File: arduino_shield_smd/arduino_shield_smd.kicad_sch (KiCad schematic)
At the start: 35 parts, among them J1 Power, J2 Digital/PWM, J3 Analog, J4 Digital/PWM, U1 ULN2803A, U2 ULN2803A, U3 PCF8574T, U4 PCF8574T

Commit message: second commit
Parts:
- added C4, C5, C6: 1uF, symbol Device:C_Small
- added D4: 2A, symbol Device:D
- added RN1, RN2, RN3, RN4: 1K, symbol Device:R_Pack04
- C2: renamed from C?; value 1uF -> 100nF
- C3: renamed from C?; value 10uF -> 22uF
- JA5: renamed from JP5; value 1X10 2.5mm -> HNC2-2.5P-10DS(55); footprint ayab-library:SHDR10W70P0X250_1X10_2740X490X590P -> ayab-library:Molex_0022035105 or Hirose_HNC2-2.5P-10DS
- R1: renamed from R3; value 100 -> 150
- R4: renamed from R1; value 5K -> 4.7K
- R5: renamed from R2; value 5K -> 4.7K
- gave numbers to parts that had none: 1
- renumbered JP2 to JA2, JP3 to JA3, JP4 to JA4, JP7 to JA7, JP8 to JA8, JP2A0 to JB2, JP3A0 to JB3, JP4A0 to JB4, JP7A0 to JB7, JP8A0 to JB8, R5 to R2, R4 to R3, U4 to U1, U1 to U4
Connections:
- net +5V: now also C5.1, C6.1, RN1.5 (R4.2), RN1.6 (R3.2), RN1.7 (R2.2), RN1.8 (R1.2), RN2.5 (R4.2), RN2.6 (R3.2), RN2.7 (R2.2), RN2.8 (R1.2), RN3.5 (R4.2), RN3.6 (R3.2), RN3.7 (R2.2), RN3.8 (R1.2), RN4.5 (R4.2), RN4.6 (R3.2), RN4.7 (R2.2), RN4.8 (R1.2)
- net GND: now also C4.2, C5.2, C6.2, D4.2 (A)
- net VIN: now also C4.1, D4.1 (K)
- net at U1.10 (P5), U2.6 (I6): now also RN2.2 (R2.1)
- net at U1.11 (P6), U2.7 (I7): now also RN2.3 (R3.1)
- net at U1.12 (P7), U2.8 (I8): now also RN2.4 (R4.1)
- net at U1.4 (P0), U2.1 (I1): now also RN1.1 (R1.1)
- net at U1.5 (P1), U2.2 (I2): now also RN1.2 (R2.1)
- net at U1.6 (P2), U2.3 (I3): now also RN1.3 (R3.1)
- net at U1.7 (P3), U2.4 (I4): now also RN1.4 (R4.1)
- net at U1.9 (P4), U2.5 (I5): now also RN2.1 (R1.1)
- net at U3.4 (P0), U4.1 (I1): now also RN3.1 (R1.1)
- net at U3.5 (P1), U4.2 (I2): now also RN3.2 (R2.1)
- net at U3.6 (P2), U4.3 (I3): now also RN3.3 (R3.1)
- net at U3.7 (P3), U4.4 (I4): now also RN3.4 (R4.1)
- net at U3.9 (P4), U4.5 (I5): now also RN4.1 (R1.1)
- net at U3.10 (P5), U4.6 (I6): now also RN4.2 (R2.1)
- net at U3.11 (P6), U4.7 (I7): now also RN4.3 (R3.1)
- net at U3.12 (P7), U4.8 (I8): now also RN4.4 (R4.1)
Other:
- note added: "JB2"
- note added: "JB3"
- note added: "JB4"
- note added: "JB7"
- note added: "JB8"
- note removed: "JP2A"
- note removed: "JP3A"
- note removed: "JP4A"
- note removed: "JP7A"
- note removed: "JP8A"
- moved on the sheet: C1, C2, C3, JA3, JA4, JA5, JA7, JA8, TP1, TP2, TP3, U1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

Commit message: OSHpark prototype
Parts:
- removed D4: 2A, symbol Device:D
- renumbered JP9 to J5, JP6 to J6
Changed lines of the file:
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@@
 	(wire
 		(pts
-			(xy 41.91 139.7) (xy 50.8 139.7)
-		)
-		(stroke
-			(width 0)
-			(type default)
-		)
-	)
-	(wire
-		(pts
 			(xy 182.88 146.05) (xy 182.88 143.51)
 		)
@@
 	(wire
 		(pts
-			(xy 41.91 132.08) (xy 50.8 132.08)
-		)
-		(stroke
-			(width 0)
-			(type default)
-		)
-	)
-	(wire
-		(pts
 			(xy 83.82 166.37) (xy 99.06 166.37)
 		)
@@
 	)
 	(symbol
-		(lib_id "Device:D")
-		(at 41.91 135.89 270)
-		(unit 1)
-		(exclude_from_sim no)
-		(in_bom yes)
-		(on_board yes)
-		(dnp no)
-		(fields_autoplaced yes)
-		(property "Reference" "D4"
-			(at 44.45 134.6199 90)
-			(effects
-				(font
-					(size 1.27 1.27)
-				)
-				(justify left)
-			)
-		)
-		(property "Value" "2A"
-			(at 44.45 137.1599 90)
-			(effects
-				(font
-					(size 1.27 1.27)
-				)
-				(justify left)
-			)
-		)
-		(property "Footprint" ""
-			(at 41.91 135.89 0)
-			(effects
-				(font
-					(size 1.27 1.27)
-				)
-				(hide yes)
-			)
-		)
-		(property "Datasheet" "~"
-			(at 41.91 135.89 0)
-			(effects
-				(font
-					(size 1.27 1.27)
-				)
-				(hide yes)
-			)
-		)
-		(property "Description" "Diode"
-			(at 41.91 135.89 0)
-			(effects
-				(font
-					(size 1.27 1.27)
-				)
-				(hide yes)
-			)
-		)
-		(property "Sim.Device" "D"
-			(at 41.91 135.89 0)
-			(effects
-				(font
-					(size 1.27 1.27)
-				)
-				(hide yes)
-			)
-		)
-		(property "Sim.Pins" "1=K 2=A"
-			(at 41.91 135.89 0)
-			(effects
-				(font
-					(size 1.27 1.27)
-				)
-				(hide yes)
-			)
-		)
-		(pin "1"
-		)
-		(pin "2"
-		)
-		(instances
-			(project ""
-				(path "/dc4e9b16-0d76-4cba-8254-625ae2e12c75"
-					(reference "D4")
-					(unit 1)
-				)
-			)
-		)
-	)
-	(symbol
 		(lib_id "ayab-lib:Conn_01x08")
 		(at 256.54 97.79 0)
@@
 		(on_board yes)
 		(dnp no)
-		(property "Reference" "JP6"
+		(property "Reference" "J6"
 			(at 107.95 63.5 90)
 			(effects
@@
 			(project ""
 				(path "/dc4e9b16-0d76-4cba-8254-625ae2e12c75"
-					(reference "JP6")
+					(reference "J6")
 					(unit 1)
 				)
@@
 		(on_board yes)
 		(dnp no)
-		(property "Reference" "JP9"
+		(property "Reference" "J5"
 			(at 237.49 135.89 0)
 			(effects
@@
 			(project ""
 				(path "/dc4e9b16-0d76-4cba-8254-625ae2e12c75"
-					(reference "JP9")
+					(reference "J5")
 					(unit 1)
 				)

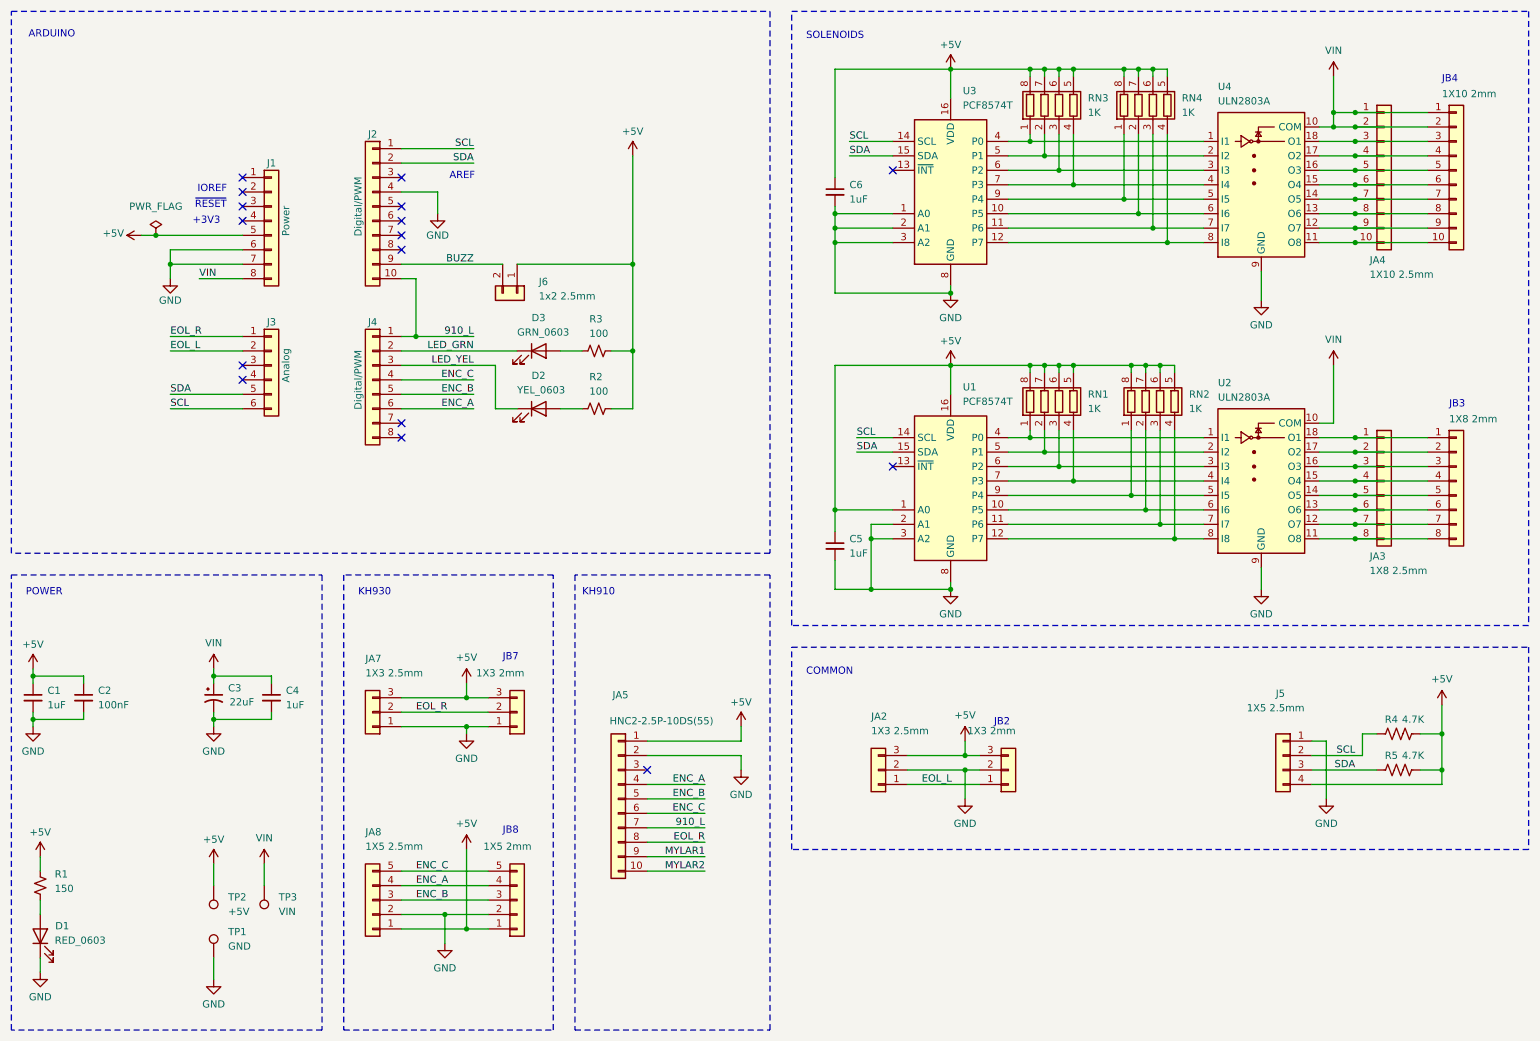
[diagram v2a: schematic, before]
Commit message: Add change LED footprints and add blue LED
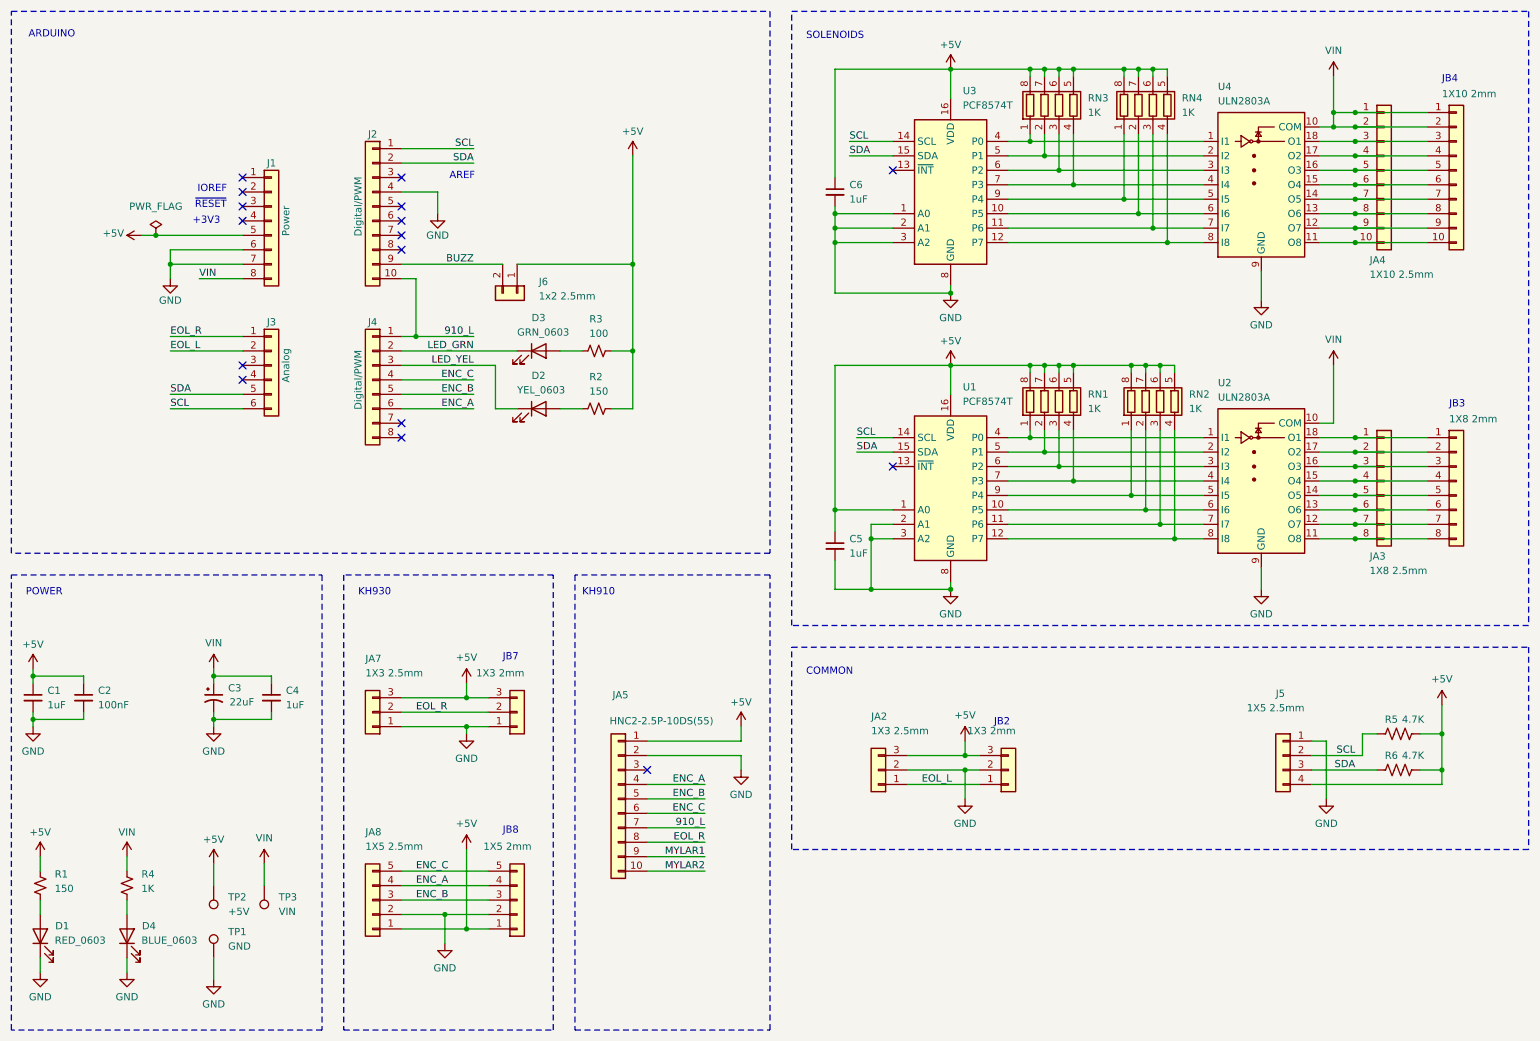
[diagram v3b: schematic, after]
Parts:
- added D4: BLUE_0603, LED_SMD:LED_0805_2012Metric, symbol ayab-lib:LED
- added R4: 1K, Resistor_SMD:R_0805_2012Metric, symbol ayab-lib:R_Small_US
- C1, C4, C5, C6: footprint (none) -> Capacitor_SMD:C_1206_3216Metric
- C2: footprint (none) -> Capacitor_SMD:C_0603_1608Metric
- C3: footprint (none) -> Capacitor_Tantalum_SMD:CP_EIA-3528-15_AVX-H
- D1: footprint LED_THT:LED_D3.0mm -> LED_SMD:LED_0805_2012Metric; Mfg Broadcom -> (none); Mfg P/N HLMP-NG07 -> (none)
- D2: footprint LED_THT:LED_D3.0mm -> LED_SMD:LED_0805_2012Metric; Mfg Broadcom -> (none); Mfg P/N HLMP-NL06 -> (none)
- D3: footprint LED_THT:LED_D3.0mm -> LED_SMD:LED_0805_2012Metric; Mfg Broadcom -> (none); Mfg P/N HLMP-1640-B00A1 -> (none)
- J1, J4: footprint Connector_PinSocket_2.54mm:PinSocket_1x08_P2.54mm_Vertical -> Connector_PinHeader_2.54mm:PinHeader_1x08_P2.54mm_Vertical
- J2: footprint Connector_PinSocket_2.54mm:PinSocket_1x10_P2.54mm_Vertical -> Connector_PinHeader_2.54mm:PinHeader_1x10_P2.54mm_Vertical
- J3: footprint Connector_PinSocket_2.54mm:PinSocket_1x06_P2.54mm_Vertical -> Connector_PinHeader_2.54mm:PinHeader_1x06_P2.54mm_Vertical
- J5: footprint Connector_PinHeader_2.54mm:PinHeader_1x04_P2.54mm_Vertical -> ayab-library:PinHeader_1x04_P2.54mm_Vertical
- J6: footprint Connector_PinHeader_2.54mm:PinHeader_1x02_P2.54mm_Vertical -> ayab-library:PinHeader_1x02_P2.54mm_Vertical
- JA2: footprint ayab-library:SHDR3W70P0X250_1X3_990X490X590P -> ayab-library:Molex_0022035035 or Hirose_HNC2-2.5P-3DS
- JA3: footprint ayab-library:SHDR8W65P0X250_1X8_2240X490X610P -> ayab-library:Molex_0022035085 or Hirose_HNC2_2.5P_8DS
- JA4: footprint ayab-library:SHDR10W70P0X250_1X10_2740X490X590P -> ayab-library:Molex_0022035105 or Hirose_HNC2-2.5P-10DS
- JA5: footprint ayab-library:Molex_0022035105 or Hirose_HNC2-2.5P-10DS -> ayab-library:HNC2-2.5P-10DS
- JA7: footprint ayab-library:SHDR3W70P0X250_1X3_990X490X590P -> ayab-library:Molex_SPOX_5267-03A_1x03_P2.50mm_Vertical
- JA8: footprint ayab-library:99990989 -> ayab-library:Molex_SPOX_5267-05A_1x05_P2.50mm_Vertical
- JB2, JB7: LCSC ID (none) -> C225241; OEM (none) -> CJT(Changjiang Connectors); OEM PN (none) -> A2004WV-3P
- JB3: LCSC ID (none) -> C225246; OEM (none) -> CJT(Changjiang Connectors); OEM PN (none) -> A2004WV-8P
- JB8: LCSC ID (none) -> C225243; OEM (none) -> CJT(Changjiang Connectors); OEM PN (none) -> A2004WV-5P
- R1, R3: footprint Resistor_THT:R_Axial_DIN0204_L3.6mm_D1.6mm_P2.54mm_Vertical -> Resistor_SMD:R_0805_2012Metric
- R2: value 100 -> 150; footprint Resistor_THT:R_Axial_DIN0204_L3.6mm_D1.6mm_P2.54mm_Vertical -> Resistor_SMD:R_0805_2012Metric
- R5: renamed from R4; footprint (none) -> Resistor_SMD:R_0805_2012Metric
- R6: renamed from R5; footprint (none) -> Resistor_SMD:R_0805_2012Metric
- RN1, RN2, RN3, RN4: footprint (none) -> Resistor_SMD:R_Array_Convex_4x0603
- TP1, TP2, TP3: footprint (none) -> TestPoint:TestPoint_THTPad_3.0x3.0mm_Drill1.5mm
- U2, U4: footprint Package_DIP:DIP-18_W7.62mm_LongPads -> Package_SO:SOIC-18W_7.5x11.6mm_P1.27mm
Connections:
- net GND: now also D4.1 (K)
- net VIN: now also R4.1
- new net: D4.2 (A), R4.2

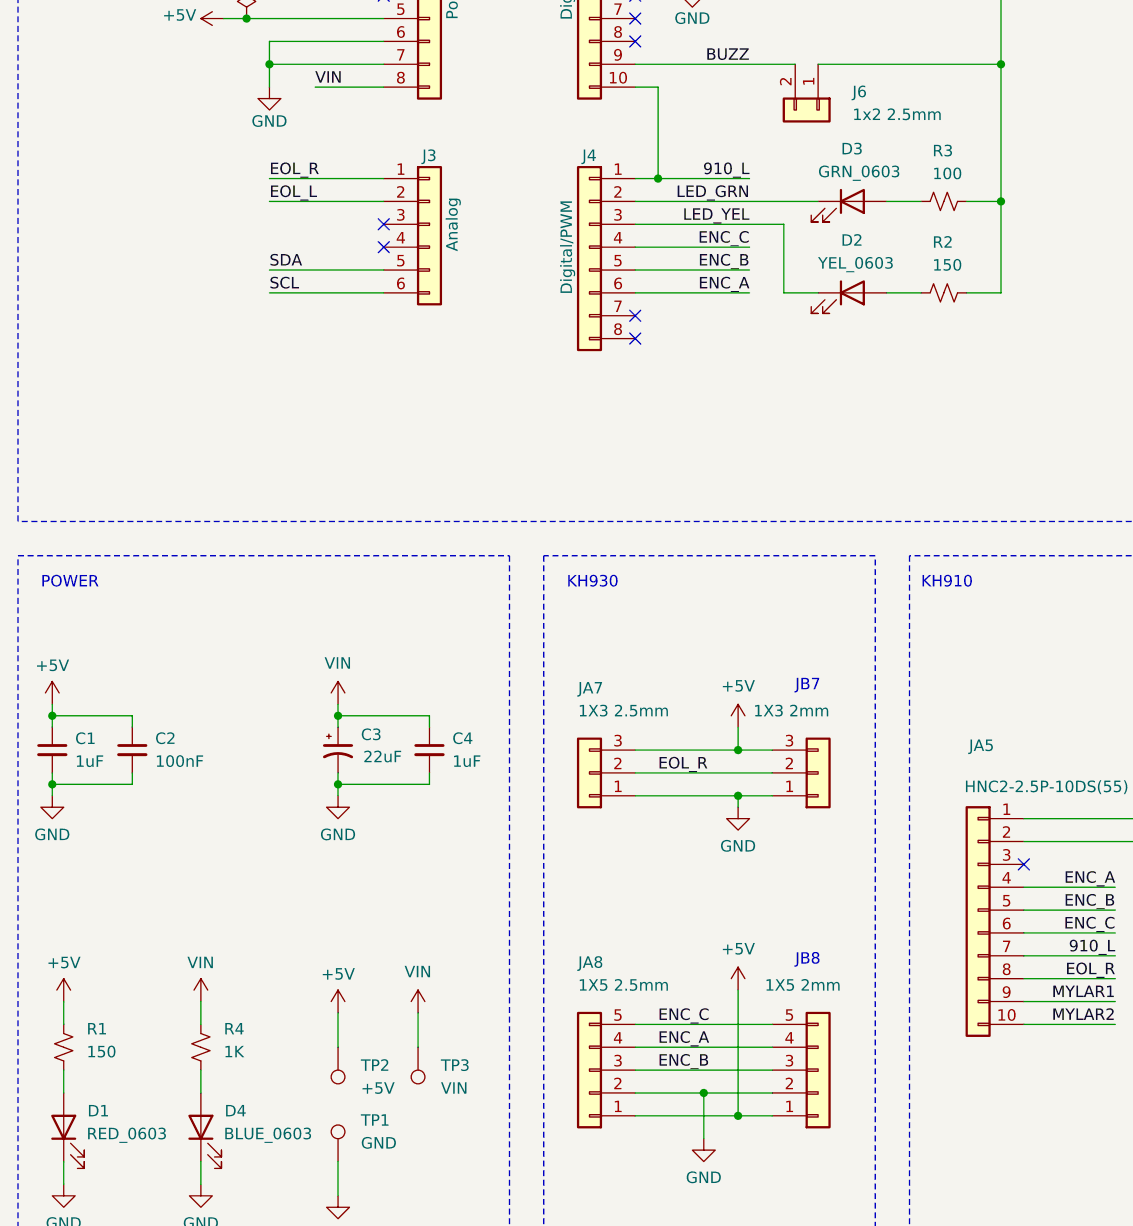
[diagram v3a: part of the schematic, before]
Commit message: Increase LED series resistor values to support Arduino Uno R4
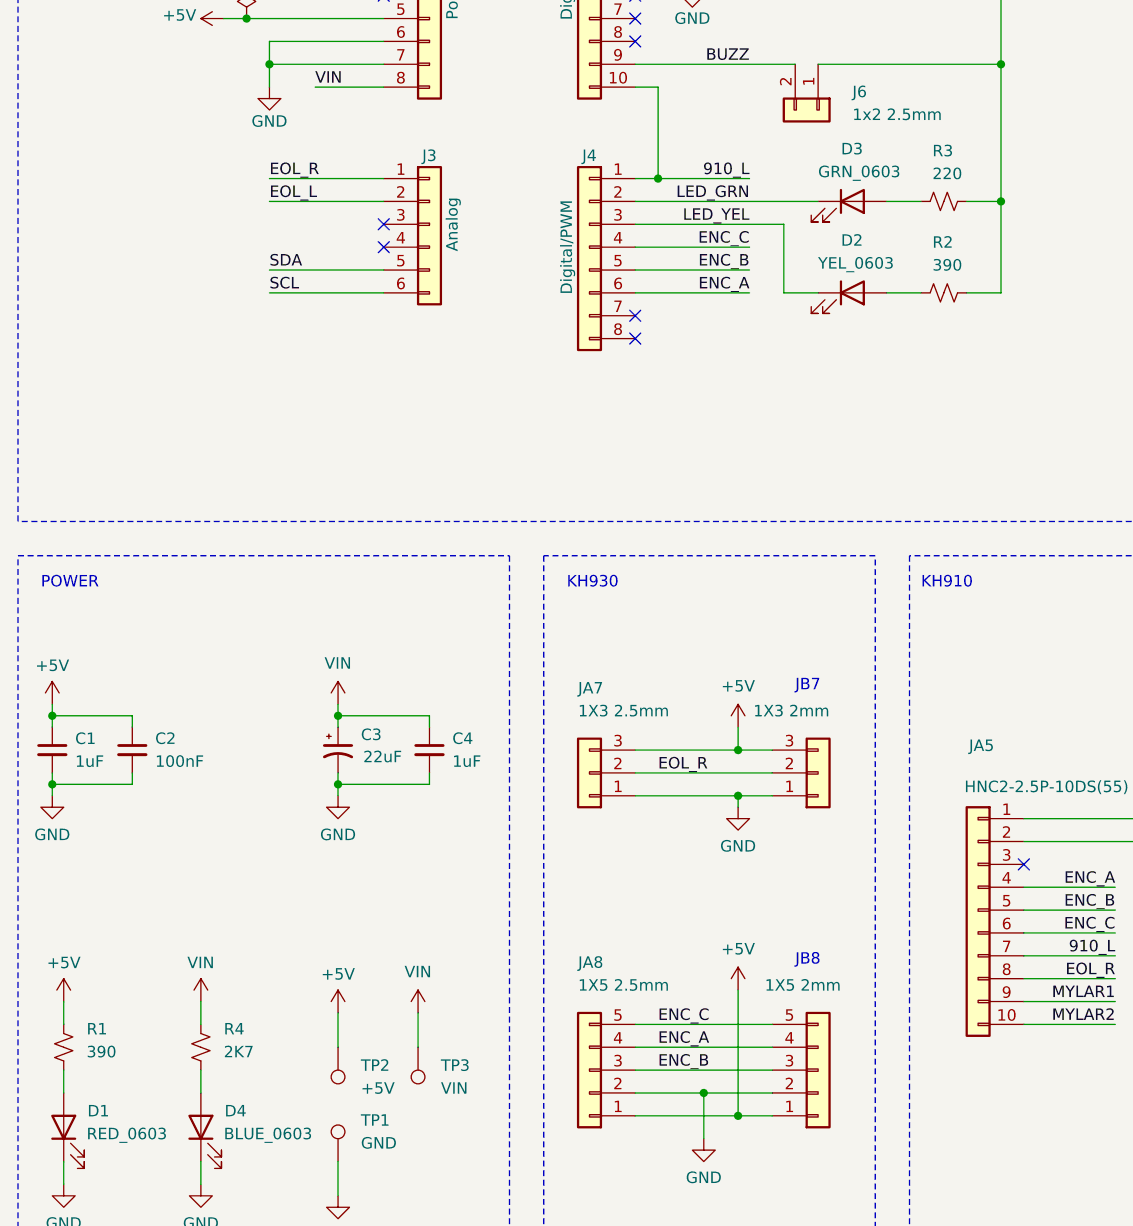
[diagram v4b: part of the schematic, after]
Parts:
- R1, R2: value 150 -> 390; Mfg Vishay -> (none); Mfg P/N RL07S151GRE6 -> (none)
- R3: value 100 -> 220; Mfg Vishay -> (none); Mfg P/N RL07S151GRE6 -> (none)
- R4: value 1K -> 2K7; Mfg Vishay -> (none); Mfg P/N RL07S151GRE6 -> (none)
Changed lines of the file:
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@@
 			)
 		)
-		(property "Value" "100"
+		(property "Value" "220"
 			(at 116.84 71.12 90)
 			(effects
@@
 			)
 		)
-		(property "Mfg" "Vishay"
+		(property "Mfg" ""
 			(at 118.11 74.93 0)
 			(effects
@@
 			)
 		)
-		(property "Mfg P/N" "RL07S151GRE6"
+		(property "Mfg P/N" ""
 			(at 118.11 74.93 0)
 			(effects
@@
 			)
 		)
-		(property "Value" "150"
+		(property "Value" "390"
 			(at 116.84 81.28 90)
 			(effects
@@
 			)
 		)
-		(property "Mfg" "Vishay"
+		(property "Mfg" ""
 			(at 118.11 85.09 0)
 			(effects
@@
 			)
 		)
-		(property "Mfg P/N" "RL07S151GRE6"
+		(property "Mfg P/N" ""
 			(at 118.11 85.09 0)
 			(effects
@@
 			)
 		)
-		(property "Value" "150"
+		(property "Value" "390"
 			(at 22.86 170.18 0)
 			(effects
@@
 			)
 		)
-		(property "Mfg" "Vishay"
+		(property "Mfg" ""
 			(at 20.32 168.91 0)
 			(effects
@@
 			)
 		)
-		(property "Mfg P/N" "RL07S151GRE6"
+		(property "Mfg P/N" ""
 			(at 20.32 168.91 0)
 			(effects
@@
 			)
 		)
-		(property "Value" "1K"
+		(property "Value" "2K7"
 			(at 38.1 170.18 0)
 			(effects
@@
 			)
 		)
-		(property "Mfg" "Vishay"
+		(property "Mfg" ""
 			(at 35.56 168.91 0)
 			(effects
@@
 			)
 		)
-		(property "Mfg P/N" "RL07S151GRE6"
+		(property "Mfg P/N" ""
 			(at 35.56 168.91 0)
 			(effects
